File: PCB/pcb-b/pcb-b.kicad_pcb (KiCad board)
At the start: 2 copper layers, 94.1 x 41.1 mm, 81 parts, among them J1 Conn_02x05_Counter_Clockwise, J2 Conn_02x04_Counter_Clockwise, K1 HK19F-DCxxV-SHC, Q1 BC817, Q11 TPCA8120,L1Q, Q13 TPCA8120,L1Q, Q14 BC817, Q15 BC817, Q19 BC817, Q2 BC817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

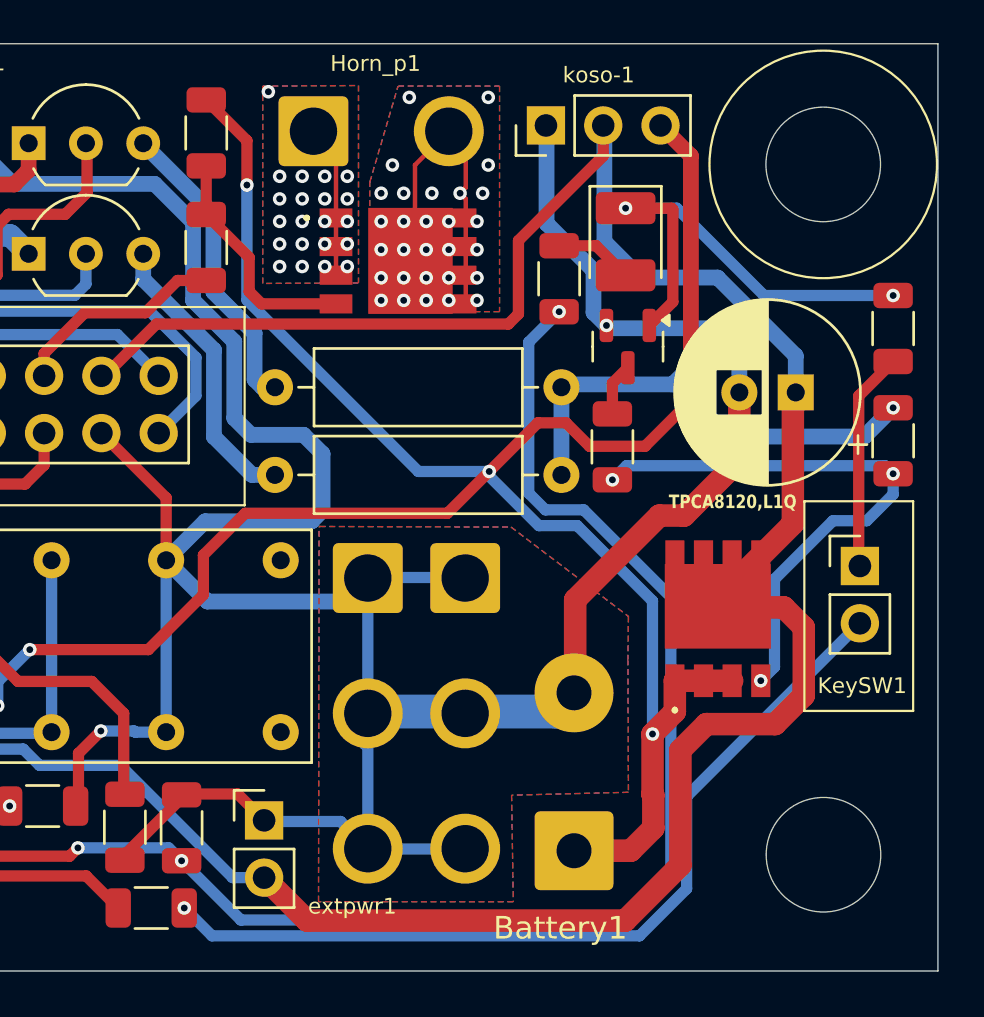
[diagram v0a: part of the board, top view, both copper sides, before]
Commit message: Enhancement for direction-indicators circuit
To make the circuit completely safe, I have added MSMF050-2 restatable-fuses to protect it vs short-circuits events.
In order to prevent PNP transistors damages, I have also added a 3 Ohm 0.5W resistor composed by four 1206 SMD componets
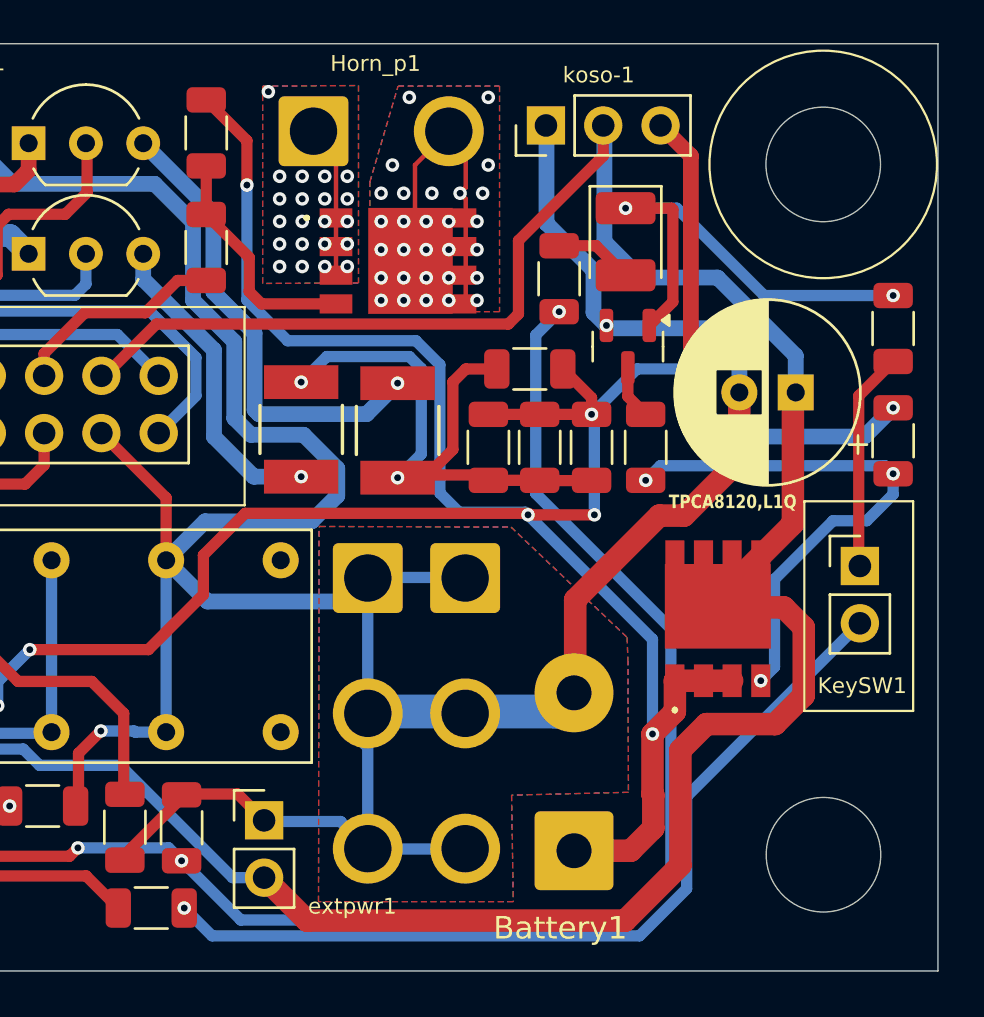
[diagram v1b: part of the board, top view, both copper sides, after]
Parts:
- added F1: MF-MSMF050-2, MSMF050-2:FUSE_F050-2, F.Cu at (172.5, 87.4)
- added F2: MF-MSMF050-2, MSMF050-2:FUSE_F050-2, F.Cu at (168.2, 87.4)
- added RA30: 12, Resistor_SMD:R_1206_3216Metric, F.Cu at (181.1, 88.2)
- added RA31: 12, Resistor_SMD:R_1206_3216Metric, F.Cu at (178.3, 84.7)
- RA23, RA29: value 10 -> 12; footprint Resistor_THT:R_Axial_DIN0309_L9.0mm_D3.2mm_P12.70mm_Horizontal -> Resistor_SMD:R_1206_3216Metric
- moved RA29 12.0 mm to (178.8, 88.2), turned to 90 degrees
- moved RA23 9.54 mm to (176.5, 88.2), turned to 90 degrees
- moved R3 1.48 mm to (183.5, 88.2)
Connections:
- RA23 pad 1: Net-(Q7-E) -> Net-(F1-Pad2)
- RA29 pad 1: Net-(Q6-E) -> Net-(F1-Pad2)
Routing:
- net Net-(F1-Pad2): track 0.00 -> 30.3 mm, vias 0 -> 2
- net Net-(Q6-E): track 13.6 -> 20.9 mm, vias 0 -> 1
- net Net-(Q13-G): track 25.3 -> 23.9 mm
- net +12V: track 217.5 -> 218.9 mm, vias 10 -> 12
- net o_keepAlive: track 76.6 -> 75.4 mm
- net Net-(Q7-E): track 12.8 -> 14.0 mm, vias 0 -> 1
- net GND: track 224.6 -> 225.1 mm

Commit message: Fixes
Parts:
- J2: value Conn_02x04_Counter_Clockwise -> Conn_02x05_Counter_Clockwise; footprint Connector_PinHeader_2.54mm:PinHeader_2x04_P2.54mm_Vertical -> Connector_PinHeader_2.54mm:PinHeader_2x05_P2.54mm_Vertical
- moved D2 5.71 mm to (151.1, 104.9), turned to 180 degrees
- moved RA39 4.11 mm to (156.3, 108.1)
- moved RA17 4.10 mm to (150.9, 108.1), turned to 180 degrees
- moved J2 0.56 mm to (132.8, 107.4)
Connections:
- J2 pad 5: c_engineOFF -> unconnected-(J2-Pin_5-Pad5)
- J2 pad 6: o_engineReady -> unconnected-(J2-Pin_6-Pad6)
- J2 pad 7: o_keepAlive -> c_engineOFF
- J2 pad 8: o_neutral -> o_engineReady
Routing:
- net Net-(Q20-B): track 19.4 -> 28.5 mm, vias 2 -> 0
- net Net-(D2-K): track 42.1 -> 34.3 mm, vias 3 -> 4
- net o_neutral: track 13.7 -> 8.34 mm
- net Net-(D2-A): track 46.0 -> 51.3 mm
- net GND: track 225.1 -> 221.7 mm, vias 16 -> 15
- net c_engineOFF: track 34.9 -> 33.0 mm
- net o_keepAlive: track 75.4 -> 73.9 mm
- net c_leftArrow: track 41.4 -> 42.7 mm
- net o_engineReady: track 8.50 -> 9.78 mm
- net +12V: track 218.9 -> 220.1 mm
- net c_rightArrow: track 29.6 -> 30.1 mm

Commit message: Small size problem fixed
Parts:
- moved RA20 0.61 mm to (131.8, 90.4)
- moved RA19 0.60 mm to (131.8, 92.8)
- moved RA21 0.60 mm to (131.8, 88.0)
- moved RA18 0.45 mm to (132.0, 95.2)
- moved RA40 0.39 mm to (132.1, 100.0)
- moved RA16 0.28 mm to (132.3, 97.6)
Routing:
- net o_engineReady: track 9.78 -> 10.6 mm
- net Net-(Q15-B): track 12.6 -> 13.2 mm
- net o_leftArrow: track 33.6 -> 34.3 mm
- net Net-(Q19-B): track 14.1 -> 14.7 mm
- net Net-(Q14-B): track 11.5 -> 12.0 mm
- net o_upLight: track 38.4 -> 38.9 mm

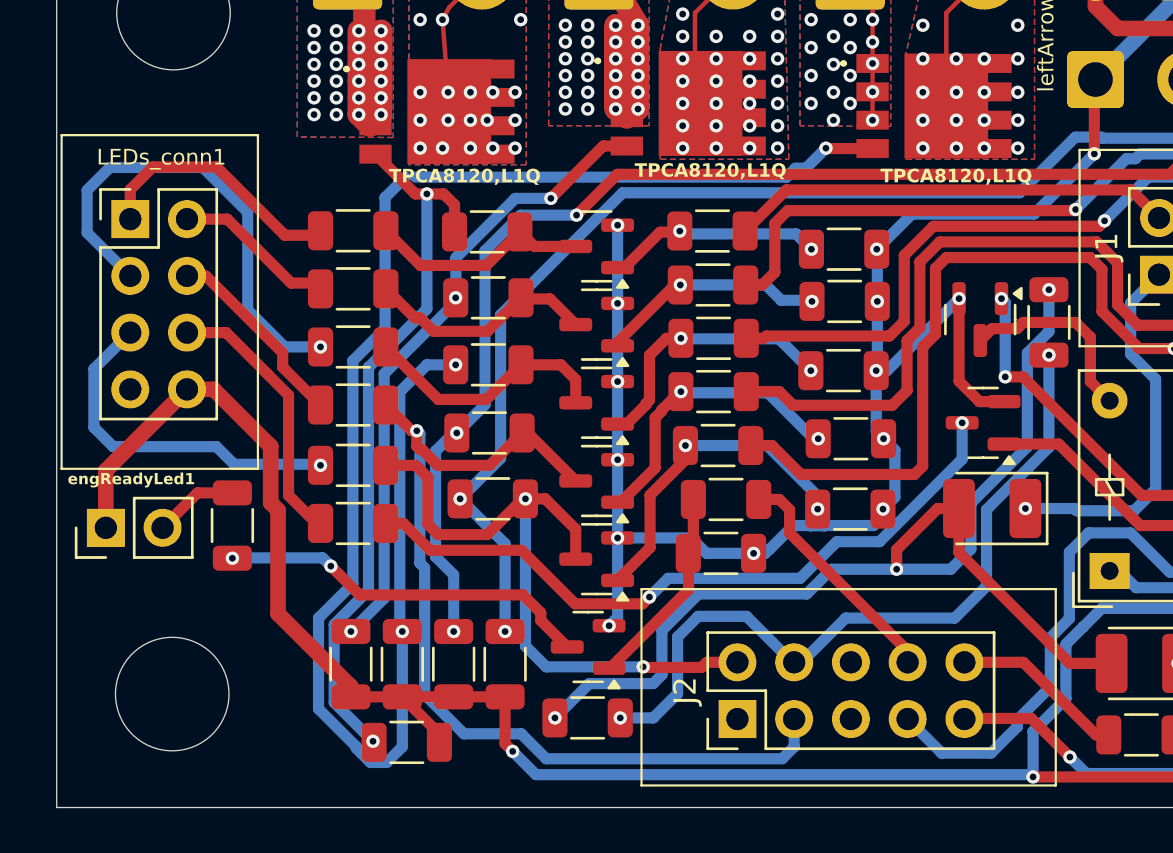
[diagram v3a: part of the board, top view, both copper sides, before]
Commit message: Fix: not common connector has been replaced
The 8-pin flat-cable connector is not easy to find on market. It has been replaced with the 10-pin standard one
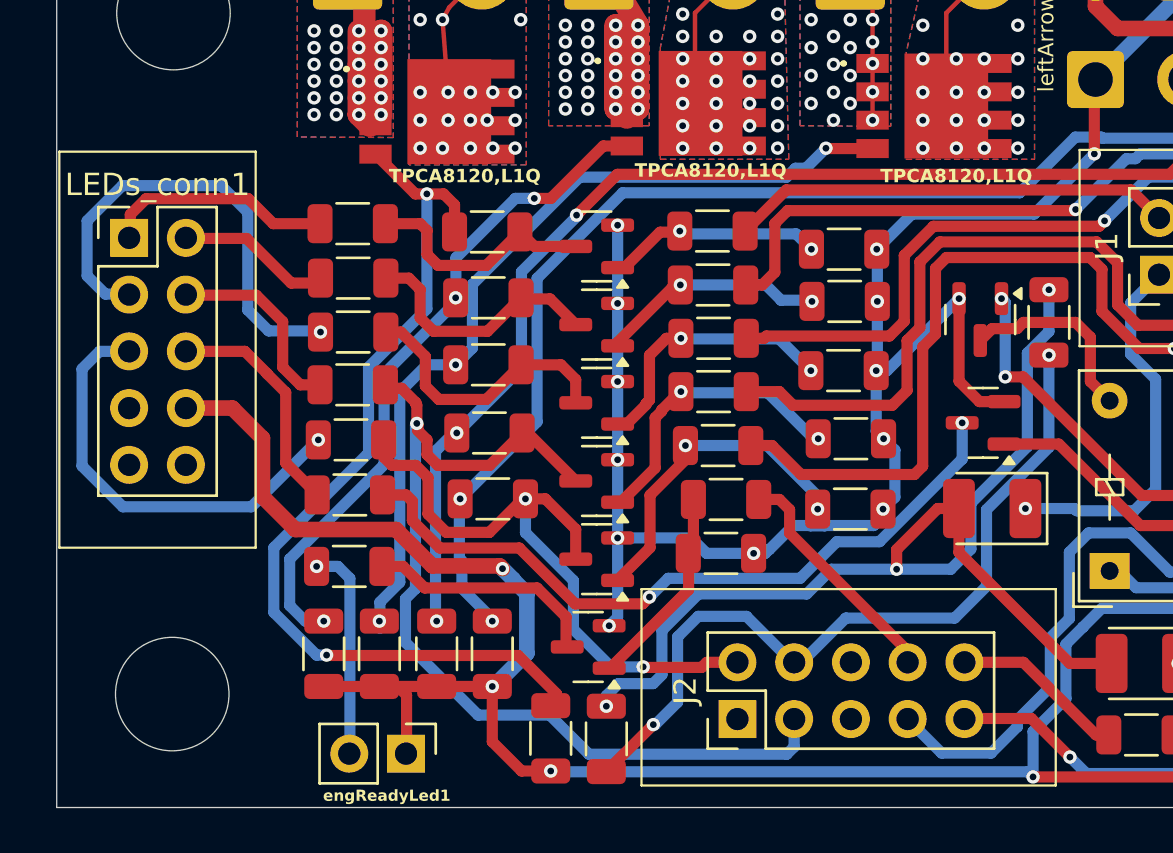
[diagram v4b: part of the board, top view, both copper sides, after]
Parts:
- LEDs_conn1: value Conn_01x08 -> Conn_02x05_Counter_Clockwise; footprint Connector_PinHeader_2.54mm:PinHeader_2x04_P2.54mm_Vertical -> Connector_PinHeader_2.54mm:PinHeader_2x05_P2.54mm_Vertical
- moved engReadyLed1 16.8 mm to (118.0, 109.0), turned to -90 degrees
- moved RA24 6.45 mm to (124.5, 108.3), turned to 90 degrees
- moved RA9 5.54 mm to (115.5, 100.6), turned to 180 degrees
- moved RA25 1.30 mm to (114.3, 104.5)
- moved RA6 1.29 mm to (115.5, 97.4)
- moved RA15 1.26 mm to (127.0, 108.3), turned to 90 degrees
- moved RA5 1.14 mm to (115.6, 94.9)
- moved RA26 1.13 mm to (116.8, 104.5)
- moved RA4 0.90 mm to (115.6, 92.4)
- moved RA27 0.89 mm to (119.4, 104.5)
- moved LEDs_conn1 0.84 mm to (105.6, 85.9)
- moved RA28 0.74 mm to (121.9, 104.5)
- moved RA3 0.67 mm to (115.7, 90.1)
- moved RA2 0.48 mm to (115.7, 87.7)
- moved RA1 0.32 mm to (115.6, 85.2)
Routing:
- net Net-(Q5-G): track 70.4 -> 38.3 mm
- net Net-(Q11-G): track 32.6 -> 42.1 mm
- net Net-(Q21-C): track 16.9 -> 10.5 mm, vias 2 -> 0
- net Net-(engReadyLed1-Pin_2): track 4.38 -> 9.57 mm, vias 0 -> 1
- net Net-(LEDs_conn1-Pin_5): track 16.3 -> 20.0 mm
- net +12V: track 220.1 -> 222.6 mm, vias 12 -> 14
- net Net-(Q6-B): track 63.0 -> 60.7 mm
- net Net-(D2-A): track 51.3 -> 49.0 mm
- net o_engineON: track 33.5 -> 35.4 mm
- net Net-(Q4-G): track 28.4 -> 30.2 mm
- net Net-(LEDs_conn1-Pin_6): track 12.1 -> 10.4 mm
- net Net-(LEDs_conn1-Pin_1): track 11.6 -> 10.3 mm
- net Net-(Q20-C): track 31.6 -> 32.8 mm
- net Net-(Q14-C): track 11.4 -> 12.5 mm
- net c_rightArrow: track 30.1 -> 29.1 mm
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
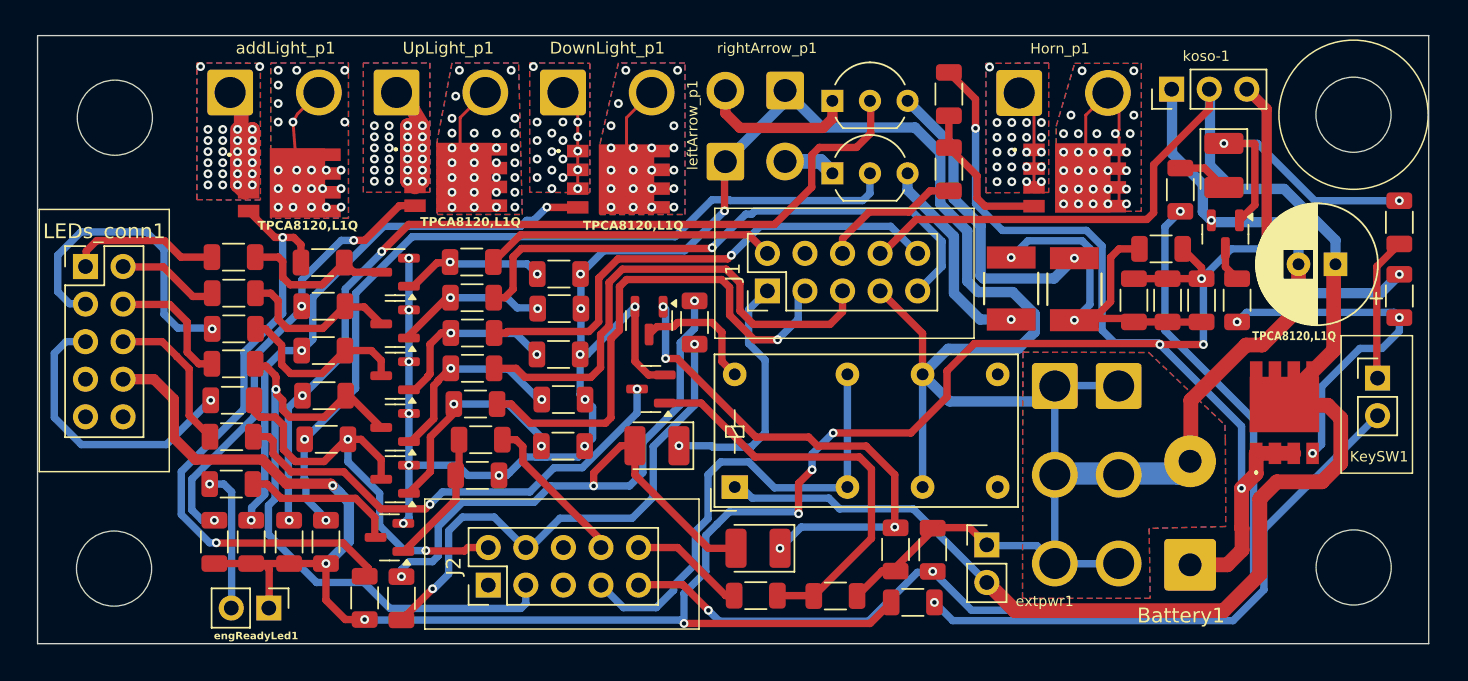
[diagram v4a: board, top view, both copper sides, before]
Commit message: Fix stupid error on the direction indicators management
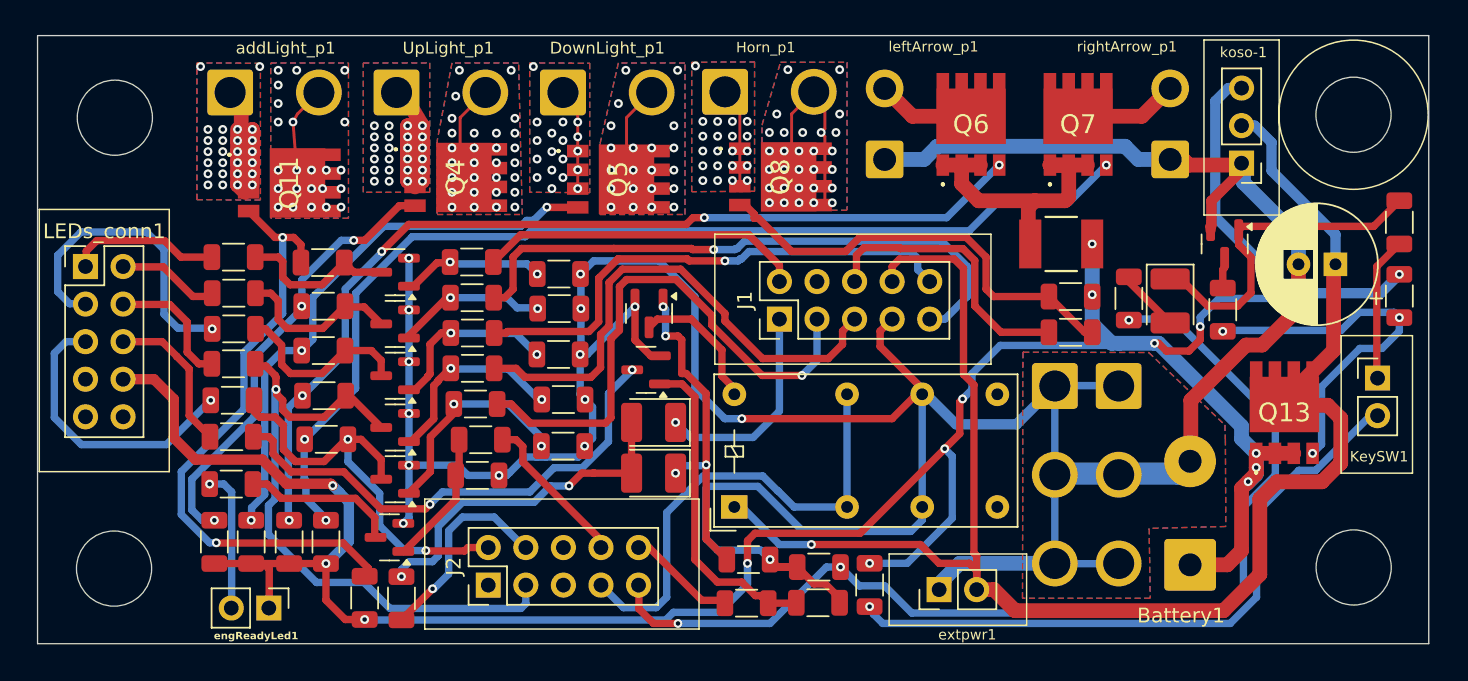
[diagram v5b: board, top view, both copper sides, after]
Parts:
- removed F1: MF-MSMF050-2, MSMF050-2:FUSE_F050-2
- removed RA23, RA29, RA30, RA31: 12, Resistor_SMD:R_1206_3216Metric
- removed RA44: 10K, Resistor_SMD:R_1206_3216Metric
- Q11, Q13, Q4, Q5, Q8: footprint TPCA8120:TPH4R003NLL1Q -> TPCA80120:TPH4R003NLL1Q
- Q6, Q7: value BC327 -> TPCA8120,L1Q; footprint Package_TO_SOT_THT:TO-92_Inline_Wide -> TPCA80120:TPH4R003NLL1Q
- RA13, RA14: value 7K -> 120
- RA9: value 0 -> 1K
- moved rightArrow_p1 26.4 mm to (179.0, 78.6), turned to 90 degrees
- moved Horn_p1 19.9 mm to (148.9, 74.1)
- moved Q8 19.9 mm to (152.6, 79.8)
- moved Q7 16.9 mm to (172.7, 76.3)
- moved RA42 16.0 mm to (172.2, 87.9), turned to 0 degrees
- moved RA7 13.8 mm to (172.2, 90.3), turned to 180 degrees
- moved leftArrow_p1 10.8 mm to (159.6, 78.6)
- moved RA8 9.97 mm to (150.4, 105.7), turned to 0 degrees
- moved D1 9.85 mm to (179.0, 88.2)
- moved Q6 9.51 mm to (165.5, 76.3)
- moved D2 8.70 mm to (144.0, 99.8)
- moved R5 8.13 mm to (176.2, 88.0)
- moved R6 7.78 mm to (155.2, 106.2), turned to 0 degrees
- moved koso-1 6.88 mm to (183.8, 78.9), turned to 180 degrees
- moved F2 4.53 mm to (171.6, 84.3), turned to 180 degrees
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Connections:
- F2 pad 1: Net-(Q7-E) -> +12V
- F2 pad 2: Net-(F1-Pad2) -> Net-(Q6-S_1)
- Q6 pad 1: Net-(Q6-C) -> Net-(Q6-S_1)
- Q6 pad 2: Net-(Q6-B) -> Net-(Q6-S_1)
- Q6 pad 3: Net-(Q6-E) -> Net-(Q6-S_1)
- Q7 pad 1: Net-(Q7-C) -> Net-(Q6-S_1)
- Q7 pad 2: Net-(Q7-B) -> Net-(Q6-S_1)
- Q7 pad 3: Net-(Q7-E) -> Net-(Q6-S_1)
- RA13 pad 2: Net-(Q6-B) -> Net-(Q6-G)
- RA14 pad 2: Net-(Q7-B) -> Net-(Q7-G)
- RA27 pad 2: Net-(Q6-B) -> Net-(Q6-G)
- RA28 pad 2: Net-(Q7-B) -> Net-(Q7-G)
- leftArrow_p1 pad 2: Net-(Q6-C) -> Net-(Q6-D_1)
- rightArrow_p1 pad 2: Net-(Q7-C) -> Net-(Q7-D_1)
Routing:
- net Net-(Q7-G): track 0.00 -> 72.0 mm, vias 0 -> 3
- net Net-(Q6-G): track 0.00 -> 65.1 mm, vias 0 -> 5
- net Net-(Q6-B): track 60.7 -> 0.00 mm, vias 3 -> 0
- net Net-(Q7-B): track 56.6 -> 0.00 mm, vias 2 -> 0
- net +12V: track 222.6 -> 192.1 mm, vias 14 -> 15
- net Net-(F1-Pad2): track 30.3 -> 0.00 mm, vias 2 -> 0
- net Net-(D2-A): track 49.0 -> 23.3 mm, vias 3 -> 2
- net o_engineON: track 35.4 -> 14.2 mm, vias 2 -> 1
- net Net-(Q6-E): track 20.9 -> 0.00 mm, vias 1 -> 0
- net Net-(Q6-S_1): track 0.00 -> 20.8 mm
- net GND: track 221.5 -> 240.7 mm
- net Net-(Q8-G): track 10.4 -> 29.6 mm
- net Net-(Q7-E): track 14.0 -> 0.00 mm, vias 1 -> 0
- net Net-(D2-K): track 34.3 -> 22.3 mm
- net Net-(Q6-C): track 10.6 -> 0.00 mm
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
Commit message: Around connectors space problems fixed
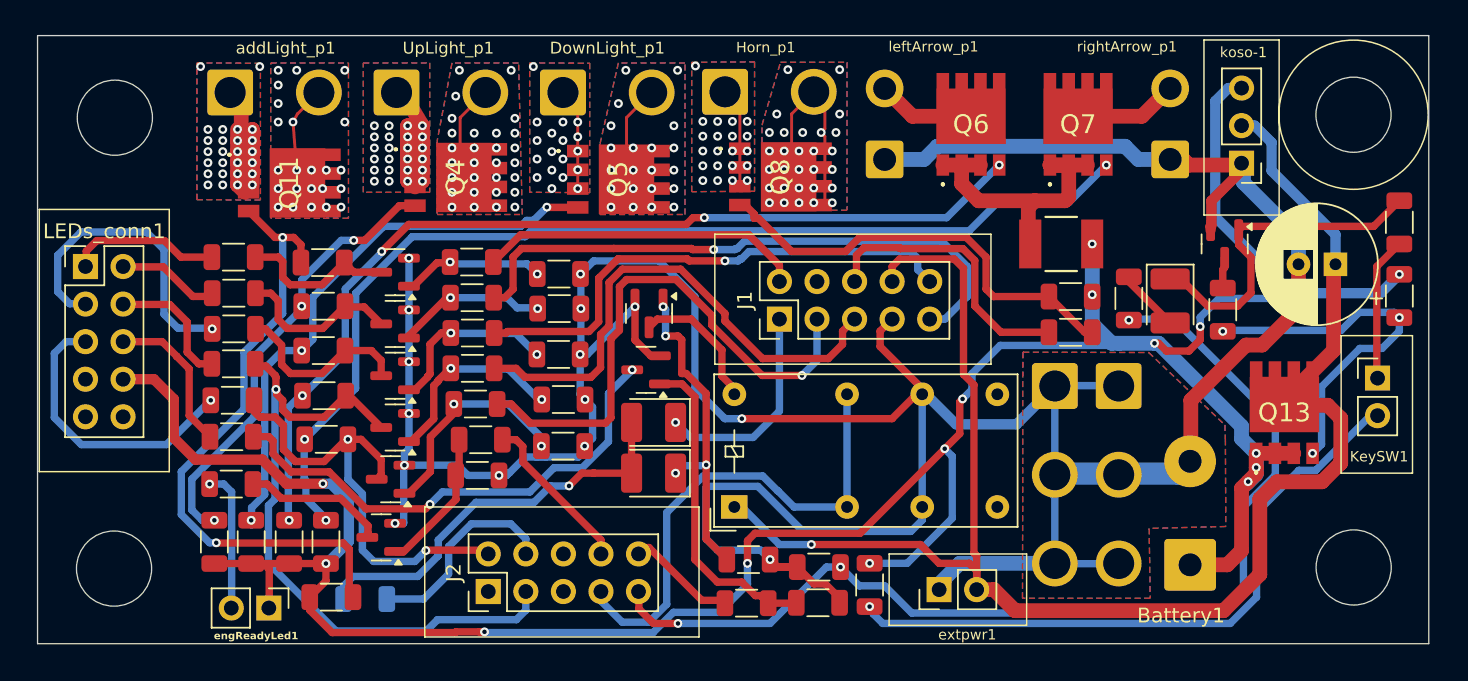
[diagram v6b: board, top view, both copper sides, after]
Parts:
- RA15: moved to B.Cu
- moved RA15 2.45 mm to (124.5, 108.3), turned to 180 degrees
- moved RA24 2.25 mm to (122.2, 108.2), turned to 0 degrees
- moved Q21 0.56 mm to (125.6, 104.2)
- moved J2 0.43 mm to (132.8, 107.8)
- moved Q19 0.30 mm to (126.2, 100.2)
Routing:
- net Net-(D2-A): track 23.3 -> 27.6 mm, vias 2 -> 1
- net c_rightArrow: track 29.1 -> 31.5 mm
- net c_leftArrow: track 43.4 -> 45.7 mm
- net c_engineOFF: track 32.8 -> 34.1 mm
- net +12V: track 192.1 -> 193.1 mm
- net Net-(Q11-G): track 42.1 -> 42.9 mm
- net GND: track 240.7 -> 241.6 mm
- net Net-(Q21-C): track 10.5 -> 9.76 mm
- net Net-(Q21-B): track 9.15 -> 9.71 mm
- net o_engineON: track 14.2 -> 14.7 mm, vias 1 -> 0
